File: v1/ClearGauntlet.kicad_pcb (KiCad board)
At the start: 2 copper layers, 1 part

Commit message: adding PCB updated with schematics
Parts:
- removed REF**: MODULE_ESP32_DEVKIT_V1, ESP32-DEVKIT-V1:MODULE_ESP32_DEVKIT_V1
- added Index1: 10k Potentiometer, Potentiometer_THT:Potentiometer_Bourns_3266Y_Vertical, F.Cu at (153.3, 65.2)
- added Index_Splay1: 10k Potentiometer, Potentiometer_THT:Potentiometer_Bourns_3266Y_Vertical, F.Cu at (153.3, 83.5)
- added M1: Motor_Servo, Potentiometer_THT:Potentiometer_Bourns_3266Y_Vertical, F.Cu at (161.6, 71.3)
- added M2: Motor_Servo, Potentiometer_THT:Potentiometer_Bourns_3266Y_Vertical, F.Cu at (169.9, 71.3)
- added M3: Motor_Servo, Potentiometer_THT:Potentiometer_Bourns_3266Y_Vertical, F.Cu at (153.3, 71.3)
- added M4: Motor_Servo, Potentiometer_THT:Potentiometer_Bourns_3266Y_Vertical, F.Cu at (178.2, 59.1)
- added M5: Motor_Servo, Potentiometer_THT:Potentiometer_Bourns_3266Y_Vertical, F.Cu at (122.7, 111.7)
- added Middle1: 10k Potentiometer, Potentiometer_THT:Potentiometer_Bourns_3266Y_Vertical, F.Cu at (161.6, 77.5)
- added Middle_Splay1: 10k Potentiometer, Potentiometer_THT:Potentiometer_Bourns_3266Y_Vertical, F.Cu at (161.6, 65.2)
- added Pink_Splay1: 10k Potentiometer, Potentiometer_THT:Potentiometer_Bourns_3266Y_Vertical, F.Cu at (161.6, 59.1)
- added Pinky1: 10k Potentiometer, Potentiometer_THT:Potentiometer_Bourns_3266Y_Vertical, F.Cu at (131.0, 111.7)
- added Ring1: 10k Potentiometer, Potentiometer_THT:Potentiometer_Bourns_3266Y_Vertical, F.Cu at (169.9, 65.2)
- added Ring_Splay1: 10k Potentiometer, Potentiometer_THT:Potentiometer_Bourns_3266Y_Vertical, F.Cu at (153.3, 77.5)
- added SW1: SW_Push, Button_Switch_SMD:SW_Push_SPST_NO_Alps_SKRK, F.Cu at (149.9, 88.9)
- added SW2: SW_Push, Button_Switch_SMD:SW_Push_SPST_NO_Alps_SKRK, F.Cu at (174.8, 64.5)
- added Thumb1: 10k Potentiometer, Potentiometer_THT:Potentiometer_Bourns_3266Y_Vertical, F.Cu at (169.9, 59.1)
- added Thumb_Splay1: 10k Potentiometer, Potentiometer_THT:Potentiometer_Bourns_3266Y_Vertical, F.Cu at (153.3, 59.1)
- added U1: ESP32-DEVKIT-V1, ESP32-DEVKIT-V1:MODULE_ESP32_DEVKIT_V1, F.Cu at (131.6, 82.4)

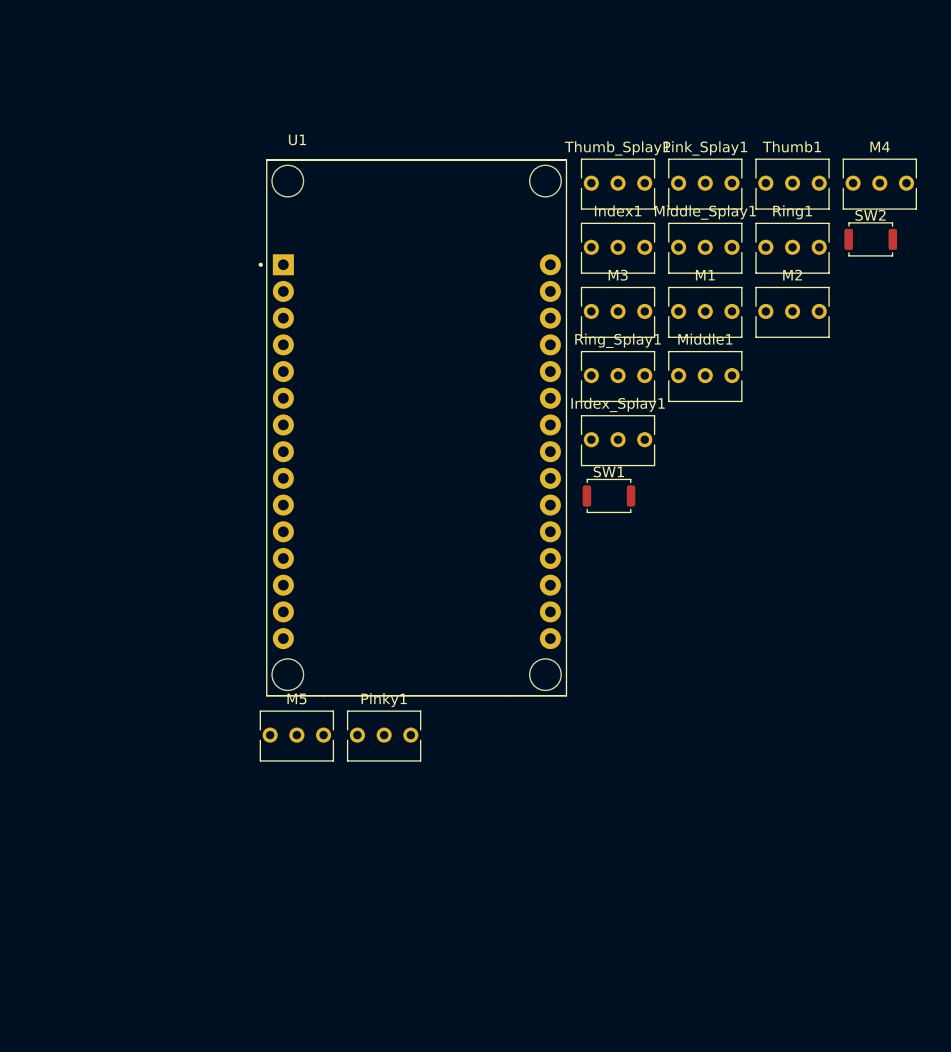
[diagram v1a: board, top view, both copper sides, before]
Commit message: PCB with wiring
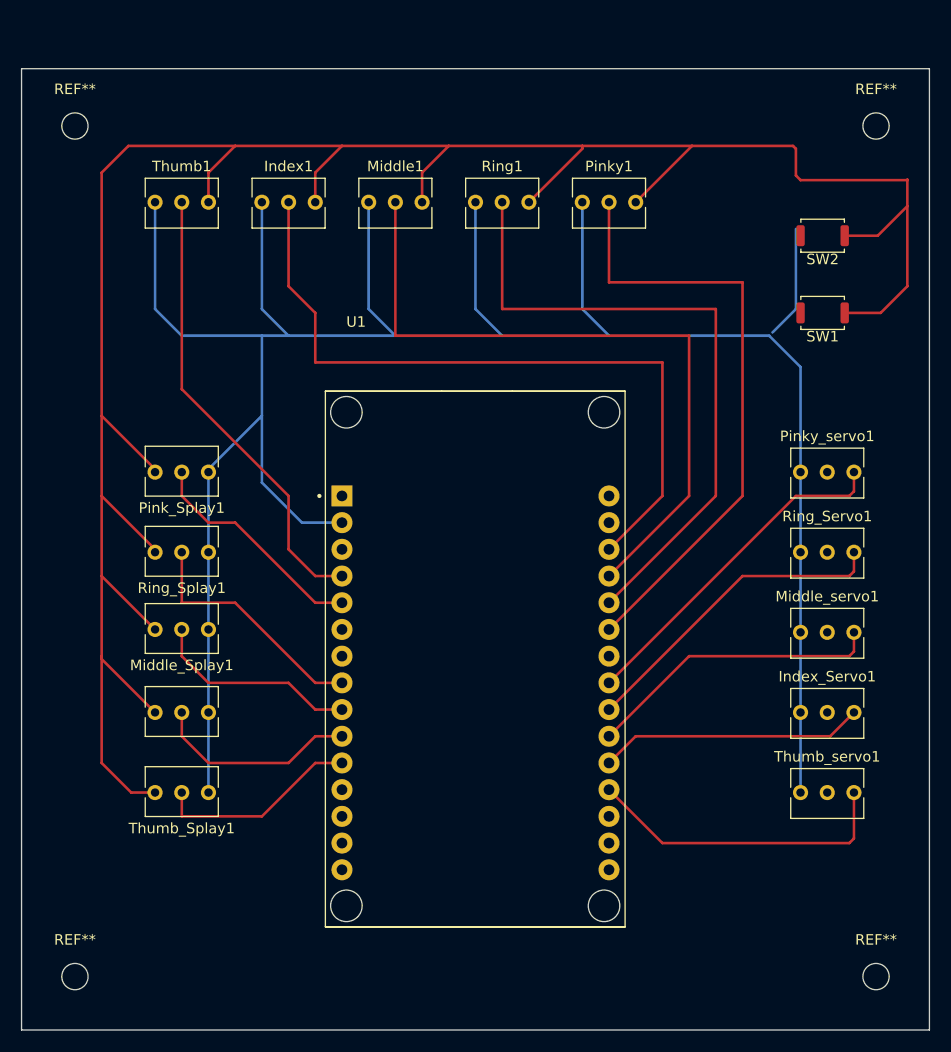
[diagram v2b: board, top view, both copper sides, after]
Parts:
- added REF**: MountingHole_2.5mm, MountingHole:MountingHole_2.5mm, F.Cu at (175.3, 134.6)
- added REF**: MountingHole_2.5mm, MountingHole:MountingHole_2.5mm, F.Cu at (99.1, 53.7)
- added REF**: MountingHole_2.5mm, MountingHole:MountingHole_2.5mm, F.Cu at (99.1, 134.6)
- added REF**: MountingHole_2.5mm, MountingHole:MountingHole_2.5mm, F.Cu at (175.3, 53.7)
- moved Thumb_Splay1 74.4 mm to (106.7, 117.1), turned to 180 degrees
- moved Middle_Splay1 65.8 mm to (106.7, 101.6), turned to 180 degrees
- moved Pink_Splay1 61.4 mm to (106.7, 86.6), turned to 180 degrees
- moved Thumb1 58.1 mm to (111.8, 61.0)
- moved Pinky1 55.0 mm to (152.4, 61.0)
- moved Index_Splay1 53.3 mm to (106.7, 109.5), turned to 180 degrees
- moved Thumb_servo1 50.7 mm to (173.2, 117.1)
- moved Index_Servo1 50.6 mm to (173.2, 109.5)
- moved Ring_Splay1 49.5 mm to (106.7, 94.3), turned to 180 degrees
- moved Middle_servo1 36.4 mm to (173.2, 101.9)
- moved Middle1 33.8 mm to (132.1, 61.0)
- moved Index1 31.6 mm to (121.9, 61.0)
- moved Ring1 28.0 mm to (142.2, 61.0)
- moved SW1 26.8 mm to (170.2, 71.5), turned to 180 degrees
- moved Ring_Servo1 23.1 mm to (173.2, 94.3)
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- renumbered M4 to Index_Servo1, M3 to Middle_servo1, M1 to Pinky_servo1, M2 to Ring_Servo1, M5 to Thumb_servo1
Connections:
- Middle_servo1 pad 1: Net-(M3-Pad1) -> Net-(U1-Pad21)
- Pinky_servo1 pad 1: Net-(M1-Pad1) -> Net-(Pinky_servo1-Pad1)
- Ring_Servo1 pad 1: Net-(M2-Pad1) -> Net-(Ring_Servo1-Pad1)
- Ring_Splay1 pad 2: Net-(Ring_Splay1-Pad2) -> Net-(U1-Pad8)
- U1 pad 21: Net-(M2-Pad1) -> Net-(U1-Pad21)
- U1 pad 22: Net-(M3-Pad1) -> Net-(Ring_Servo1-Pad1)
- U1 pad 23: unconnected-(U1-Pad23) -> Net-(Pinky_servo1-Pad1)
- U1 pad 25: Net-(M1-Pad1) -> Net-(Pinky1-Pad2)
- U1 pad 26: Net-(Pink_Splay1-Pad2) -> Net-(Ring1-Pad2)
- U1 pad 27: Net-(Index1-Pad2) -> Net-(Middle1-Pad2)
- U1 pad 28: Net-(Thumb1-Pad2) -> Net-(Index1-Pad2)
- U1 pad 3: Net-(Ring_Splay1-Pad2) -> unconnected-(U1-Pad3)
- U1 pad 4: Net-(Pinky1-Pad2) -> Net-(Thumb1-Pad2)
- U1 pad 5: Net-(Ring1-Pad2) -> Net-(Pink_Splay1-Pad2)
- U1 pad 8: Net-(Middle1-Pad2) -> Net-(U1-Pad8)
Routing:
- net Net-(Index1-Pad1): track 0.00 -> 230.4 mm
- net GND: track 0.00 -> 230.4 mm
- net Net-(Index1-Pad2): track 0.00 -> 69.2 mm
- net Net-(Middle1-Pad2): track 0.00 -> 66.7 mm
- net Net-(Ring1-Pad2): track 0.00 -> 62.6 mm
- net Net-(Pinky1-Pad2): track 0.00 -> 58.6 mm
- net Net-(Thumb1-Pad2): track 0.00 -> 43.4 mm
- net Net-(Pinky_servo1-Pad1): track 0.00 -> 32.7 mm
- net Net-(Ring_Servo1-Pad1): track 0.00 -> 30.6 mm
- net Net-(Thumb_servo1-Pad1): track 0.00 -> 30.0 mm
- net Net-(U1-Pad21): track 0.00 -> 28.5 mm
- net Net-(Index_Servo1-Pad1): track 0.00 -> 25.3 mm
- net Net-(U1-Pad8): track 0.00 -> 23.2 mm
- net Net-(Pink_Splay1-Pad2): track 0.00 -> 21.7 mm
- net Net-(Middle_Splay1-Pad2): track 0.00 -> 19.9 mm
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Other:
- board outline added: 86.4 x 91.4 mm

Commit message: adding v3
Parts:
- added REF**: PinHeader_1x03_P1.00mm_Vertical, Connector_PinHeader_1.00mm:PinHeader_1x03_P1.00mm_Vertical, F.Cu at (162.6, 127.0)
- added REF**: PinHeader_1x03_P1.00mm_Vertical, Connector_PinHeader_1.00mm:PinHeader_1x03_P1.00mm_Vertical, F.Cu at (157.5, 127.0)
- moved REF** 98.9 mm to (147.3, 48.3)
- moved REF** 87.7 mm to (160.0, 48.3)
- moved REF** 46.0 mm to (129.5, 48.3)
- moved REF** 16.2 mm to (114.3, 48.3)
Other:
- board size 86.4 x 91.4 mm -> 78.7 x 78.7 mm
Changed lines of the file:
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@@
     (property "Sheetname" "")
     (attr through_hole)
-    (fp_text reference "Index_Splay1" (at -2.54 -3.41) (layer "B.SilkS")
-      (effects (font (size 1 1) (thickness 0.15)) (justify mirror))
+    (fp_text reference "Index_Splay1" (at -2.54 -3.41 180) (layer "F.SilkS")
+      (effects (font (size 1 1) (thickness 0.15)))
     )
     (fp_text value "10k Potentiometer" (at -2.54 3.59) (layer "F.Fab")
@@
   )
   (footprint "MountingHole:MountingHole_2.5mm" (layer "F.Cu")
-    (at 175.26 134.62)
+    (at 160.02 48.26)
     (descr "Mounting Hole 2.5mm, no annular")
     (tags "mounting hole 2.5mm no annular")
@@
   )
   (footprint "MountingHole:MountingHole_2.5mm" (layer "F.Cu")
-    (at 99.06 53.71)
+    (at 114.3 48.26)
     (descr "Mounting Hole 2.5mm, no annular")
     (tags "mounting hole 2.5mm no annular")
@@
       (net 3 "GND") (pinfunction "3") (pintype "passive"))
     (model "${KICAD6_3DMODEL_DIR}/Potentiometer_THT.3dshapes/Potentiometer_Bourns_3266Y_Vertical.wrl"
+      (offset (xyz 0 0 0))
+      (scale (xyz 1 1 1))
+      (rotate (xyz 0 0 0))
+    )
+  )
+  (footprint "Connector_PinHeader_1.00mm:PinHeader_1x03_P1.00mm_Vertical" (layer "F.Cu")
+    (at 162.56 127)
+    (descr "Through hole straight pin header, 1x03, 1.00mm pitch, single row")
+    (tags "Through hole pin header THT 1x03 1.00mm single row")
+    (attr through_hole)
+    (fp_text reference "REF**" (at 0 -1.56) (layer "F.SilkS")
+      (effects (font (size 1 1) (thickness 0.15)))
+    )
+    (fp_text value "PinHeader_1x03_P1.00mm_Vertical" (at 0 3.56) (layer "F.Fab")
+      (effects (font (size 1 1) (thickness 0.15)))
+    )
+    (fp_text user "${REFERENCE}" (at 0 1 90) (layer "F.Fab")
+      (effects (font (size 0.76 0.76) (thickness 0.114)))
+    )
+    (fp_line (start -0.695 2.56) (end -0.394493 2.56) (layer "F.SilkS") (width 0.12))
+    (fp_line (start -0.695 -0.685) (end 0 -0.685) (layer "F.SilkS") (width 0.12))
+    (fp_line (start 0.394493 2.56) (end 0.695 2.56) (layer "F.SilkS") (width 0.12))
+    (fp_line (start 0.695 0.685) (end 0.695 2.56) (layer "F.SilkS") (width 0.12))
+    (fp_line (start 0.608276 0.685) (end 0.695 0.685) (layer "F.SilkS") (width 0.12))
+    (fp_line (start -0.695 0) (end -0.695 -0.685) (layer "F.SilkS") (width 0.12))
+    (fp_line (start -0.695 0.685) (end -0.695 2.56) (layer "F.SilkS") (width 0.12))
+    (fp_line (start -0.695 0.685) (end -0.608276 0.685) (layer "F.SilkS") (width 0.12))
+    (fp_line (start 1.15 3) (end 1.15 -1) (layer "F.CrtYd") (width 0.05))
+    (fp_line (start 1.15 -1) (end -1.15 -1) (layer "F.CrtYd") (width 0.05))
+    (fp_line (start -1.15 -1) (end -1.15 3) (layer "F.CrtYd") (width 0.05))
+    (fp_line (start -1.15 3) (end 1.15 3) (layer "F.CrtYd") (width 0.05))
+    (fp_line (start -0.635 2.5) (end -0.635 -0.1825) (layer "F.Fab") (width 0.1))
+    (fp_line (start -0.635 -0.1825) (end -0.3175 -0.5) (layer "F.Fab") (width 0.1))
+    (fp_line (start 0.635 -0.5) (end 0.635 2.5) (layer "F.Fab") (width 0.1))
+    (fp_line (start 0.635 2.5) (end -0.635 2.5) (layer "F.Fab") (width 0.1))
+    (fp_line (start -0.3175 -0.5) (end 0.635 -0.5) (layer "F.Fab") (width 0.1))
+    (pad "1" thru_hole rect (at 0 0) (size 0.85 0.85) (drill 0.5) (layers *.Cu *.Mask))
+    (pad "2" thru_hole oval (at 0 1) (size 0.85 0.85) (drill 0.5) (layers *.Cu *.Mask))
+    (pad "3" thru_hole oval (at 0 2) (size 0.85 0.85) (drill 0.5) (layers *.Cu *.Mask))
+    (model "${KICAD6_3DMODEL_DIR}/Connector_PinHeader_1.00mm.3dshapes/PinHeader_1x03_P1.00mm_Vertical.wrl"
       (offset (xyz 0 0 0))
       (scale (xyz 1 1 1))
@@
   )
   (footprint "MountingHole:MountingHole_2.5mm" (layer "F.Cu")
-    (at 99.06 134.62)
+    (at 147.32 48.26)
     (descr "Mounting Hole 2.5mm, no annular")
     (tags "mounting hole 2.5mm no annular")
@@
     )
   )
+  (footprint "Connector_PinHeader_1.00mm:PinHeader_1x03_P1.00mm_Vertical" (layer "F.Cu")
+    (at 157.48 127)
+    (descr "Through hole straight pin header, 1x03, 1.00mm pitch, single row")
+    (tags "Through hole pin header THT 1x03 1.00mm single row")
+    (attr through_hole)
+    (fp_text reference "REF**" (at 0 -1.56) (layer "F.SilkS")
+      (effects (font (size 1 1) (thickness 0.15)))
+    )
+    (fp_text value "PinHeader_1x03_P1.00mm_Vertical" (at 0 3.56) (layer "F.Fab")
+      (effects (font (size 1 1) (thickness 0.15)))
+    )
+    (fp_text user "${REFERENCE}" (at 0 1 90) (layer "F.Fab")
+      (effects (font (size 0.76 0.76) (thickness 0.114)))
+    )
+    (fp_line (start -0.695 0) (end -0.695 -0.685) (layer "F.SilkS") (width 0.12))
+    (fp_line (start -0.695 2.56) (end -0.394493 2.56) (layer "F.SilkS") (width 0.12))
+    (fp_line (start 0.608276 0.685) (end 0.695 0.685) (layer "F.SilkS") (width 0.12))
+    (fp_line (start 0.695 0.685) (end 0.695 2.56) (layer "F.SilkS") (width 0.12))
+    (fp_line (start -0.695 0.685) (end -0.608276 0.685) (layer "F.SilkS") (width 0.12))
+    (fp_line (start 0.394493 2.56) (end 0.695 2.56) (layer "F.SilkS") (width 0.12))
+    (fp_line (start -0.695 0.685) (end -0.695 2.56) (layer "F.SilkS") (width 0.12))
+    (fp_line (start -0.695 -0.685) (end 0 -0.685) (layer "F.SilkS") (width 0.12))
+    (fp_line (start 1.15 3) (end 1.15 -1) (layer "F.CrtYd") (width 0.05))
+    (fp_line (start 1.15 -1) (end -1.15 -1) (layer "F.CrtYd") (width 0.05))
+    (fp_line (start -1.15 3) (end 1.15 3) (layer "F.CrtYd") (width 0.05))
+    (fp_line (start -1.15 -1) (end -1.15 3) (layer "F.CrtYd") (width 0.05))
+    (fp_line (start 0.635 -0.5) (end 0.635 2.5) (layer "F.Fab") (width 0.1))
+    (fp_line (start -0.3175 -0.5) (end 0.635 -0.5) (layer "F.Fab") (width 0.1))
+    (fp_line (start -0.635 -0.1825) (end -0.3175 -0.5) (layer "F.Fab") (width 0.1))
+    (fp_line (start 0.635 2.5) (end -0.635 2.5) (layer "F.Fab") (width 0.1))
+    (fp_line (start -0.635 2.5) (end -0.635 -0.1825) (layer "F.Fab") (width 0.1))
+    (pad "1" thru_hole rect (at 0 0) (size 0.85 0.85) (drill 0.5) (layers *.Cu *.Mask))
+    (pad "2" thru_hole oval (at 0 1) (size 0.85 0.85) (drill 0.5) (layers *.Cu *.Mask))
+    (pad "3" thru_hole oval (at 0 2) (size 0.85 0.85) (drill 0.5) (layers *.Cu *.Mask))
+    (model "${KICAD6_3DMODEL_DIR}/Connector_PinHeader_1.00mm.3dshapes/PinHeader_1x03_P1.00mm_Vertical.wrl"
+      (offset (xyz 0 0 0))
+      (scale (xyz 1 1 1))
+      (rotate (xyz 0 0 0))
+    )
+  )
   (footprint "Potentiometer_THT:Potentiometer_Bourns_3266Y_Vertical" (layer "F.Cu")
     (at 106.68 117.115 180)
@@
       (effects (font (size 1 1) (thickness 0.15)))
     )
-    (fp_text value "10k Potentiometer" (at -2.54 3.59) (layer "F.Fab")
+    (fp_text value "10k Potentiometer" (at -2.54 3.59 180) (layer "F.Fab")
       (effects (font (size 1 1) (thickness 0.15)))
     )
@@
   )
   (footprint "MountingHole:MountingHole_2.5mm" (layer "F.Cu")
-    (at 175.26 53.71)
+    (at 129.54 48.26)
     (descr "Mounting Hole 2.5mm, no annular")
     (tags "mounting hole 2.5mm no annular")
@@
   (gr_poly
     (pts
-      (xy 180.34 139.7)
-      (xy 93.98 139.7)
-      (xy 93.98 48.26)
-      (xy 180.34 48.26)
+      (xy 177.8 132.08)
+      (xy 99.06 132.08)
+      (xy 99.06 53.34)
+      (xy 177.8 53.34)
     ) (layer "Edge.Cuts") (width 0.1) (fill none))
   (segment (start 167.64 71.12) (end 165.418198 73.341802) (width 0.25) (layer "B.Cu") (net 0))
